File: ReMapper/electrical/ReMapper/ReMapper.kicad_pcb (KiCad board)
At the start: 4 copper layers, 95.8 x 48.2 mm, 51 parts, among them J2 USB_IN, J5 USB_OUT, U1 ESP32-S3-WROOM-1-N8R8, U2 RP2040, U3 W25Q128JVE, U4 RT6150B-33GQW, U5 W25Q128JVE, Y1 12MHZ

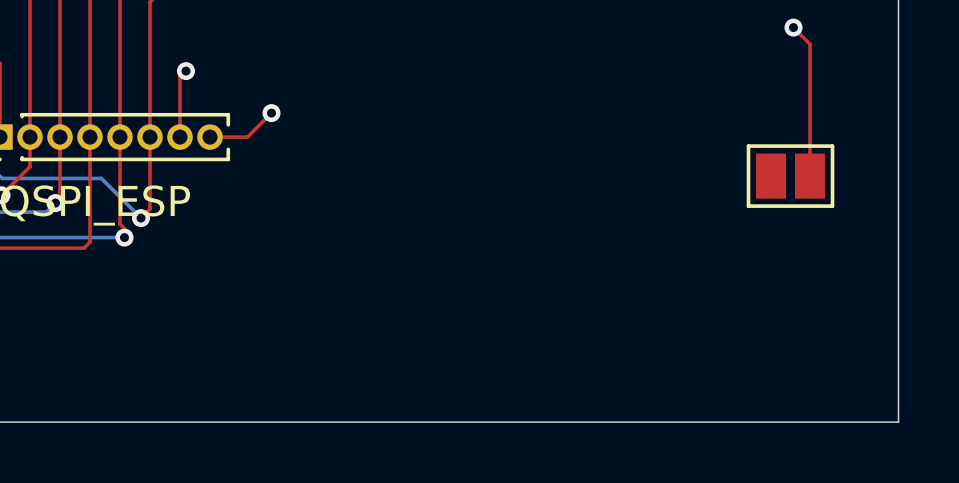
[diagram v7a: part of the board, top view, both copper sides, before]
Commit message: low lcsc inventory on some parts, switch to standard lib instead of extended for them. for the Crystal and Boost Convertor
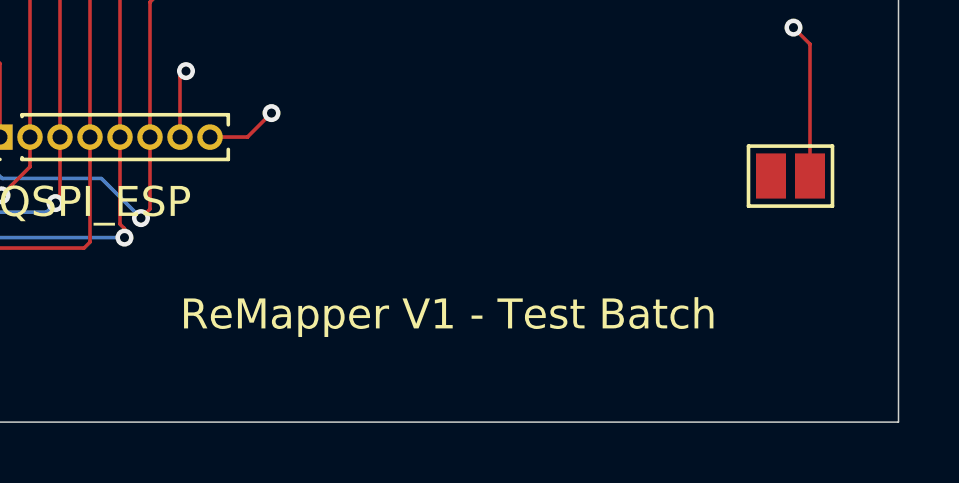
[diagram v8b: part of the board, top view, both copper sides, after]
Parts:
- R5, R7, R8: value 400 -> 500
- R6: value 800 -> 500
- renumbered 33V_led1 to LED1, USB_led1 to LED2, rp_led1 to LED3, esp_led1 to LED4
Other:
- board text added: "ReMapper V1 - Test Batch"
